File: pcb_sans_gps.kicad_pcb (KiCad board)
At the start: 2 copper layers, 42.5 x 43 mm, 16 parts, among them J1 Conn_01x20, J2 USB_B_Micro, J3 Conn_01x02, U2 ESP32-C6-MINI-1/U

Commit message: Avec connecteur femelle pour GPS
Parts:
- added J4: Conn_01x05, Connector_PinSocket_2.54mm:PinSocket_1x05_P2.54mm_Vertical, F.Cu at (112.2, 135.5)
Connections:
- U2 pad 19: unconnected-(U2-GPIO14-Pad19) -> Net-(J4-Pin_4)
- U2 pad 20: unconnected-(U2-GPIO15-Pad20) -> Net-(J4-Pin_3)
- U2 pad 22: unconnected-(U2-GPIO8-Pad22) -> Net-(J4-Pin_5)
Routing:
- net Net-(J4-Pin_5): track 0.00 -> 19.2 mm, vias 0 -> 1
- net Net-(J4-Pin_4): track 0.00 -> 18.6 mm, vias 0 -> 1
- net Net-(J4-Pin_3): track 0.00 -> 15.5 mm, vias 0 -> 1
- net /ALIM 3V3: track 72.5 -> 84.0 mm
- net GND: track 16.7 -> 19.7 mm, vias 7 -> 8

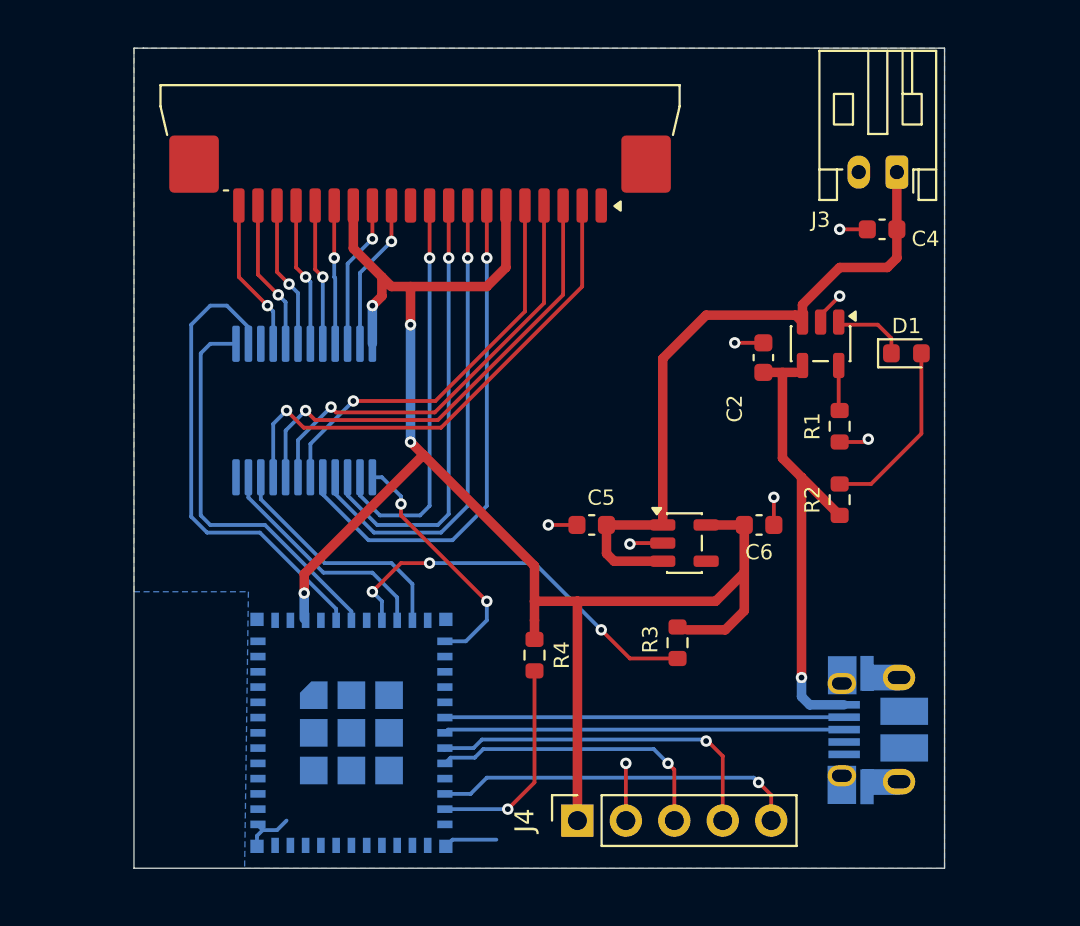
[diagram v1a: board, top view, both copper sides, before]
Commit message: Projet complet - GPS avec Pin Socket et Mounting Holes
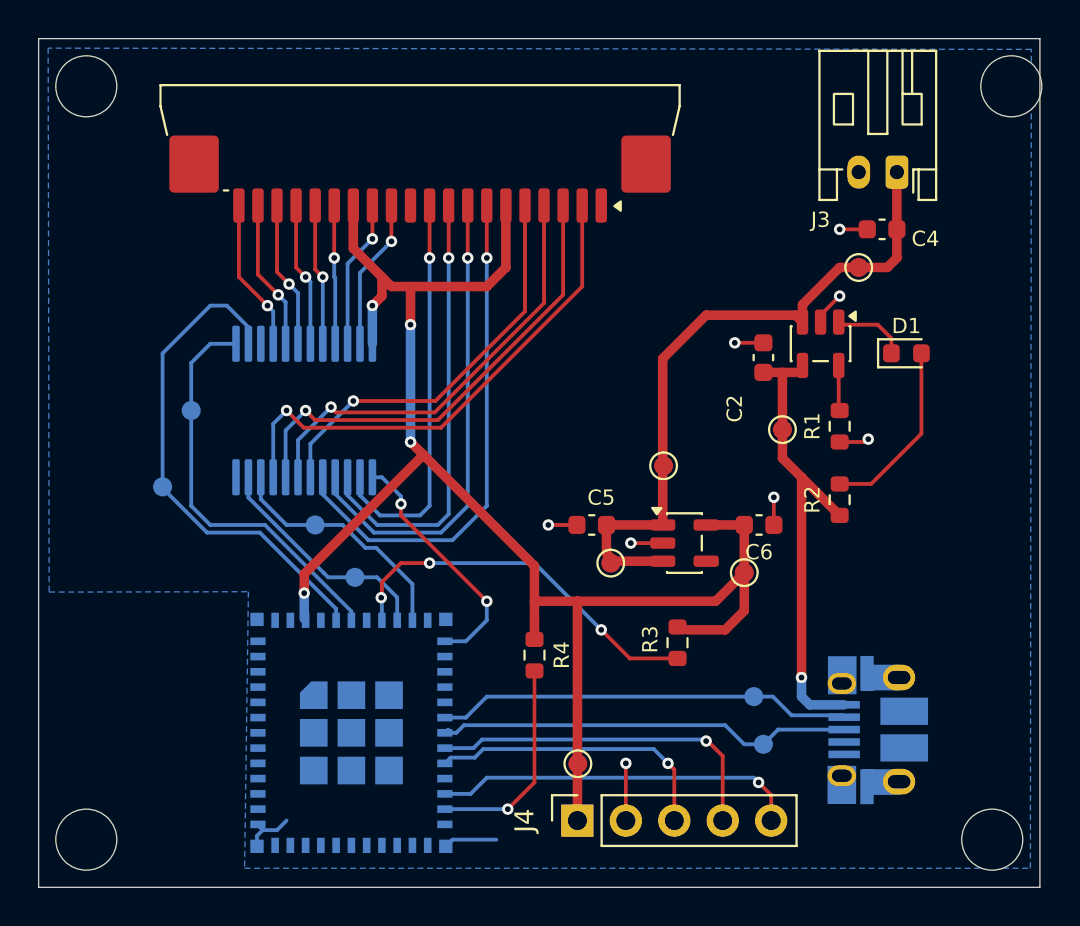
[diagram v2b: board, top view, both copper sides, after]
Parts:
- added H1: MountingHole, MountingHole:MountingHole_3.2mm_M3, F.Cu at (86.5, 97.0)
- added H2: MountingHole, MountingHole:MountingHole_3.2mm_M3, F.Cu at (135.0, 97.0)
- added H3: MountingHole, MountingHole:MountingHole_3.2mm_M3, F.Cu at (86.5, 136.5)
- added H4: MountingHole, MountingHole:MountingHole_3.2mm_M3, F.Cu at (134.0, 136.5)
- added TP10: TestPoint, TestPoint:TestPoint_Pad_D1.0mm, B.Cu at (98.5, 120.0)
- added TP15: TestPoint, TestPoint:TestPoint_Pad_D1.0mm, F.Cu at (121.0, 122.5)
- added TP17: TestPoint, TestPoint:TestPoint_Pad_D1.0mm, F.Cu at (127.0, 106.5)
- added TP19: TestPoint, TestPoint:TestPoint_Pad_D1.0mm, F.Cu at (116.8, 116.9)
- added TP20: TestPoint, TestPoint:TestPoint_Pad_D1.0mm, F.Cu at (114.0, 122.0)
- added TP22: TestPoint, TestPoint:TestPoint_Pad_D1.0mm, F.Cu at (123.0, 115.0)
- added TP24: TestPoint, TestPoint:TestPoint_Pad_D1.0mm, F.Cu at (112.3, 132.5)
- added TP4: TestPoint, TestPoint:TestPoint_Pad_D1.0mm, B.Cu at (122.0, 131.5)
- added TP5: TestPoint, TestPoint:TestPoint_Pad_D1.0mm, B.Cu at (121.5, 129.0)
- added TP7: TestPoint, TestPoint:TestPoint_Pad_D1.0mm, B.Cu at (90.5, 118.0)
- added TP8: TestPoint, TestPoint:TestPoint_Pad_D1.0mm, B.Cu at (92.0, 114.0)
- added TP9: TestPoint, TestPoint:TestPoint_Pad_D1.0mm, B.Cu at (100.6, 122.7)
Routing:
- net Net-(MUX1-S2): track 25.0 -> 26.3 mm
- net Net-(J2-D+): track 21.0 -> 22.1 mm
- net Net-(J2-D-): track 20.9 -> 21.8 mm
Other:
- board size 42.5 x 43 mm -> 52.5 x 44.5 mm
